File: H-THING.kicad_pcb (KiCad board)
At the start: 2 copper layers, 18 parts, among them J1 MOTOR_CON, J2 PWR_PASSTHRU, J3 MAIN_PWR, J4 SIG_CON, Q1 2N3904, Q2 IRF5305, Q3 HUF75321, Q4 IRF5305, Q5 HUF75321, Q6 2N3904

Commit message: Layed out PCB
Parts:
- removed R3: 0R00, Resistors_THT:R_Axial_DIN0207_L6.3mm_D2.5mm_P2.54mm_Vertical
- added R6: 0R20, Resistors_THT:R_Axial_DIN0207_L6.3mm_D2.5mm_P2.54mm_Vertical, F.Cu at (161.8, 112.0)
- added REF**: MountingHole_3.2mm_M3, Mounting_Holes:MountingHole_3.2mm_M3, F.Cu at (168.8, 113.5)
- added REF**: MountingHole_3.2mm_M3, Mounting_Holes:MountingHole_3.2mm_M3, F.Cu at (168.8, 91.4)
- added REF**: MountingHole_3.2mm_M3, Mounting_Holes:MountingHole_3.2mm_M3, F.Cu at (143.4, 113.4)
- added REF**: MountingHole_3.2mm_M3, Mounting_Holes:MountingHole_3.2mm_M3, F.Cu at (143.5, 91.4)
- C1, C3: footprint Capacitors_THT:C_Disc_D3.4mm_W2.1mm_P2.50mm -> Capacitors_THT:C_Disc_D5.0mm_W2.5mm_P5.00mm
- C2: footprint Capacitors_SMD:CP_Elec_8x10.5 -> Capacitors_THT:CP_Radial_D10.0mm_P5.00mm
- J1, J2, J3: footprint TerminalBlocks_Phoenix:TerminalBlock_Phoenix_MPT-2.54mm_2pol -> Connectors_Terminal_Blocks:TerminalBlock_bornier-2_P5.08mm
- J4: footprint Connectors_JST:JST_XH_B03B-XH-A_03x2.50mm_Straight -> Socket_Strips:Socket_Strip_Straight_1x03_Pitch2.54mm
- Q1, Q6: footprint TO_SOT_Packages_THT:TO-92_Molded_Narrow -> TO_SOT_Packages_THT:TO-92_Inline_Narrow_Oval
- Q2, Q3, Q4, Q5: footprint TO_SOT_Packages_THT:TO-220-3_Horizontal -> TO_SOT_Packages_THT:TO-220-3_Vertical
- R2, R4: value 3k30 -> 1k00
- moved Q1 33.1 mm to (157.1, 114.0), turned to 90 degrees
- moved C1 32.2 mm to (149.4, 100.5), turned to 270 degrees
- moved R1 31.4 mm to (151.4, 114.4), turned to 180 degrees
- moved J3 31.1 mm to (175.5, 113.5)
- moved J1 29.3 mm to (143.5, 100.3), turned to 270 degrees
- moved C2 29.1 mm to (175.6, 103.9)
- moved C3 28.7 mm to (175.6, 96.8)
- moved J2 27.2 mm to (180.6, 90.9), turned to 180 degrees
- moved Q3 26.2 mm to (169.7, 105.2), turned to 180 degrees
- moved R2 21.1 mm to (149.4, 111.0), turned to 0 degrees
- moved Q5 17.3 mm to (164.6, 100.6), turned to 0 degrees
- moved J4 14.5 mm to (162.8, 89.8)
- moved Q2 12.5 mm to (159.0, 105.2), turned to 180 degrees
- moved Q6 7.87 mm to (150.7, 90.9), turned to 270 degrees
- moved R5 7.10 mm to (157.9, 90.3), turned to 180 degrees
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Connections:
- J1 pad 1: Net-(C1-Pad2) -> Net-(C1-Pad1)
- J1 pad 2: Net-(C1-Pad1) -> Net-(C1-Pad2)
- J2 pad 1: VCC -> GND
- J2 pad 2: GND -> VCC
- J4 pad 2: GND -> /I_SENSE
- Q3 pad 3: GND -> /I_SENSE
- Q5 pad 3: GND -> /I_SENSE
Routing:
- net VCC: track 0.00 -> 63.3 mm
- net /HB1: track 0.00 -> 42.0 mm
- net Net-(C1-Pad1): track 0.00 -> 31.7 mm
- net Net-(C1-Pad2): track 0.00 -> 31.6 mm
- net /I_SENSE: track 0.00 -> 27.8 mm
- net Net-(Q1-Pad3): track 0.00 -> 25.8 mm
- net Net-(Q4-Pad1): track 0.00 -> 24.9 mm
- net /HB2: track 0.00 -> 6.85 mm
- net Net-(Q1-Pad2): track 0.00 -> 6.40 mm
- net Net-(Q6-Pad2): track 0.00 -> 5.36 mm
- added copper zone on B.Cu, net GND
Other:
- board outline added: 44.6 x 31 mm

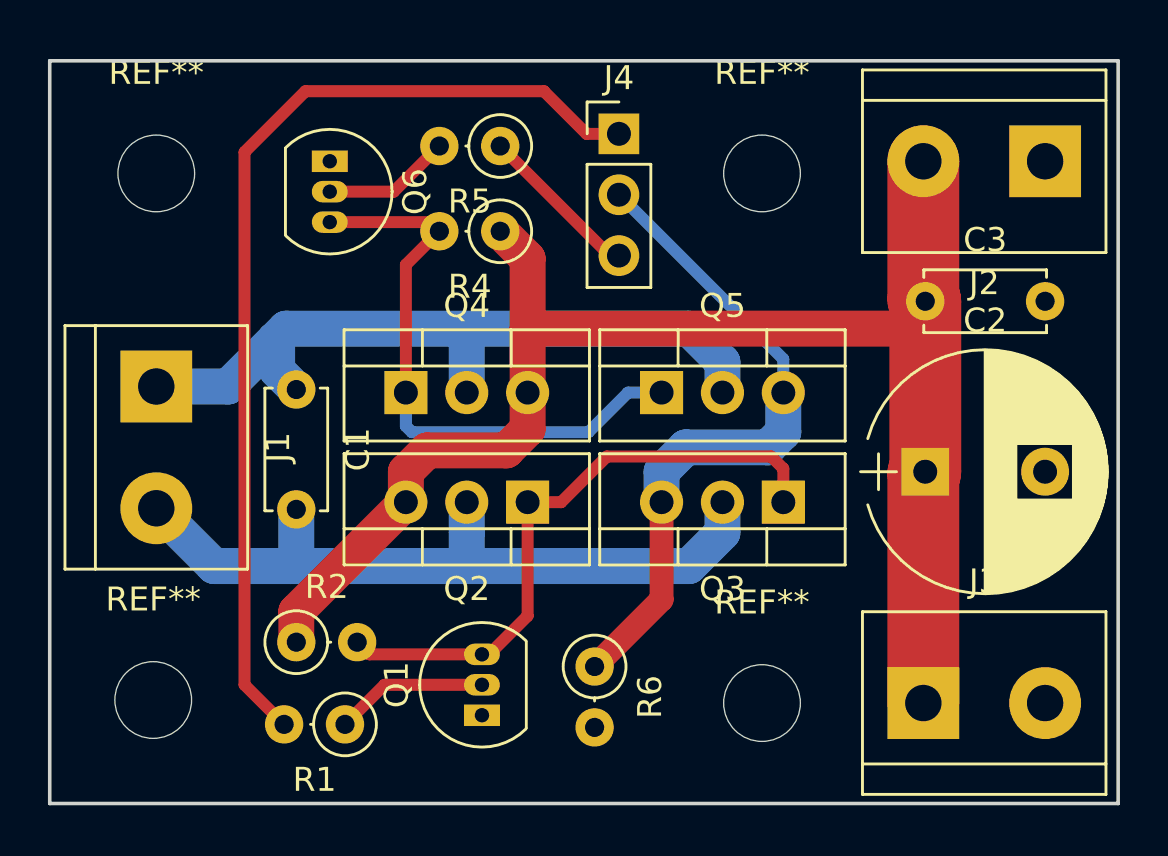
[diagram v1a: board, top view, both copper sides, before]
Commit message: Added images
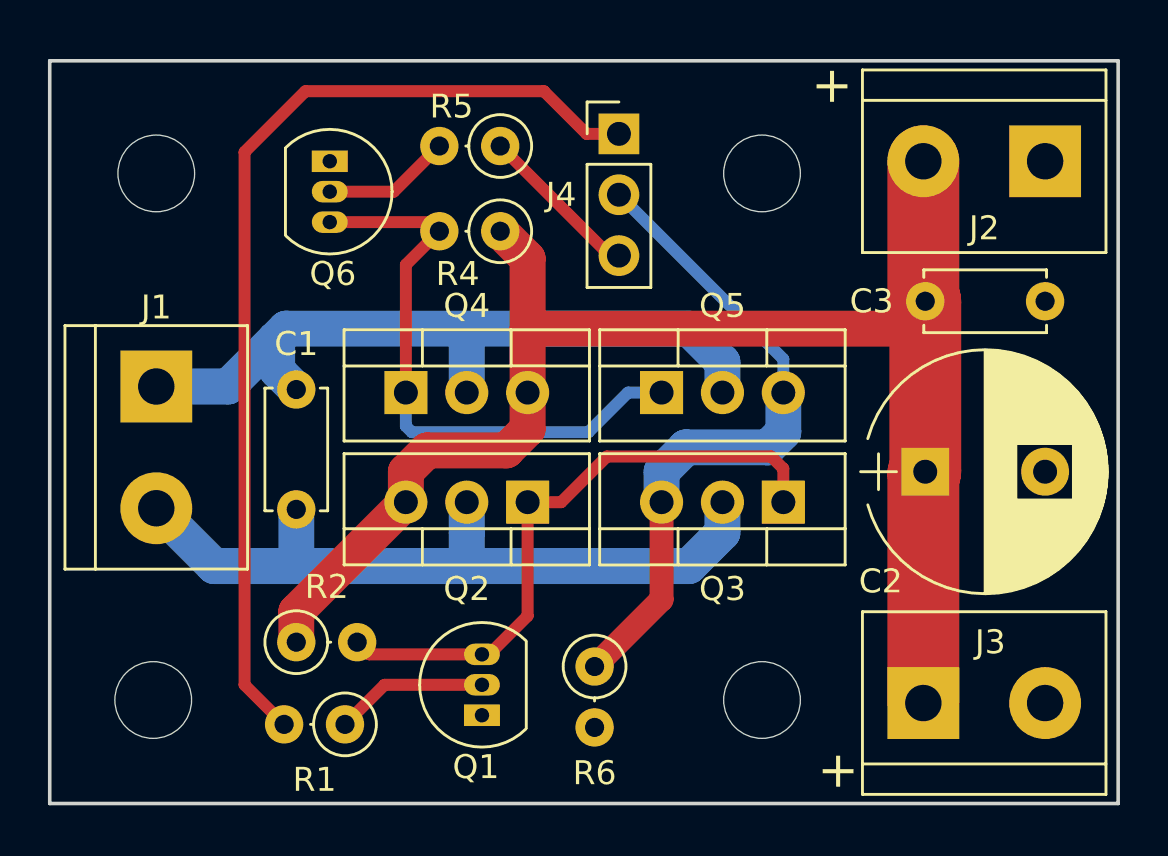
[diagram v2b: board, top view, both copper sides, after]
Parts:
- added G***: LOGO, footprints:rover, B.Cu at (161.9, 108.8)
- moved MH3 0.13 mm to (168.8, 113.4)
- turned MH1 to 180 degrees
- turned MH2 to 180 degrees
- renumbered REF** to MH1, REF** to MH2, REF** to MH3, REF** to MH4
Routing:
- added copper zone on F.Cu, net GND
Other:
- board text added: "+"
- board text added: "H-THING (H-Bridge) by Vlad Pomogaev"

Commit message: Added propper grbr outputs
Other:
- board text added: "MOTOR"
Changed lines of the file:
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@@
   (general
     (thickness 1.6)
-    (drawings 12)
+    (drawings 13)
     (tracks 79)
     (zones 0)
@@
   (page A4)
   (layers
-    (0 F.Cu signal)
-    (31 B.Cu signal)
+    (0 F.Cu signal hide)
+    (31 B.Cu signal hide)
     (32 B.Adhes user)
     (33 F.Adhes user)
@@
     (pad_to_mask_clearance 0.2)
     (aux_axis_origin 0 0)
-    (visible_elements 7FFEEFFF)
+    (visible_elements 7FFFEFFF)
     (pcbplotparams
-      (layerselection 0x00030_80000001)
+      (layerselection 0x010f0_ffffffff)
       (usegerberextensions false)
       (usegerberattributes false)
@@
       (outputformat 1)
       (mirror false)
-      (drillshape 1)
+      (drillshape 0)
       (scaleselection 1)
       (outputdirectory ""))
@@
       (xy -1.910234 -1.966072) (xy -1.841807 -1.920478) (xy -1.827096 -1.934329)) (layer B.SilkS) (width 0.01))
   )
+  (gr_text MOTOR (at 143.5354 109.1438) (layer F.SilkS)
+    (effects (font (size 1.5 1.5) (thickness 0.3)))
+  )
   (dimension 14.732 (width 0.3) (layer Dwgs.User)

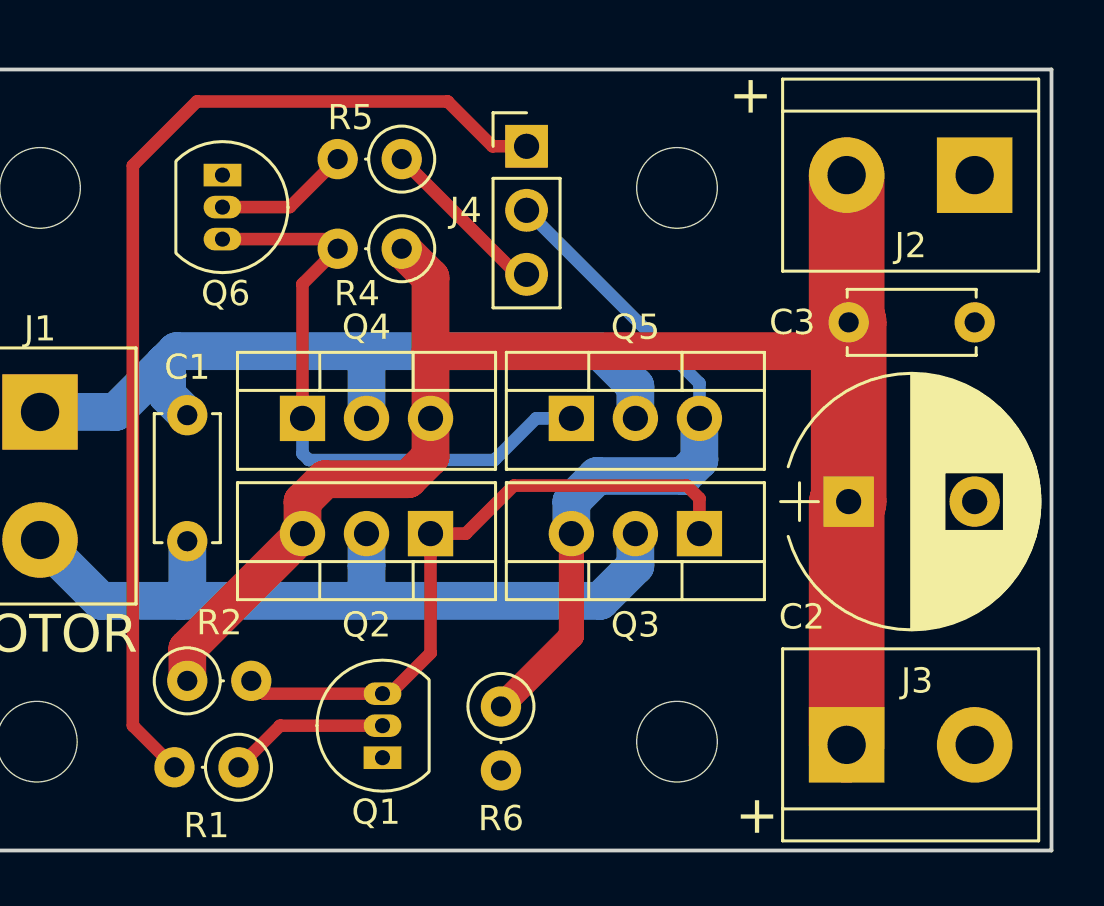
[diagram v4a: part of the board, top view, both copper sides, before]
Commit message: Updated 3d model with components
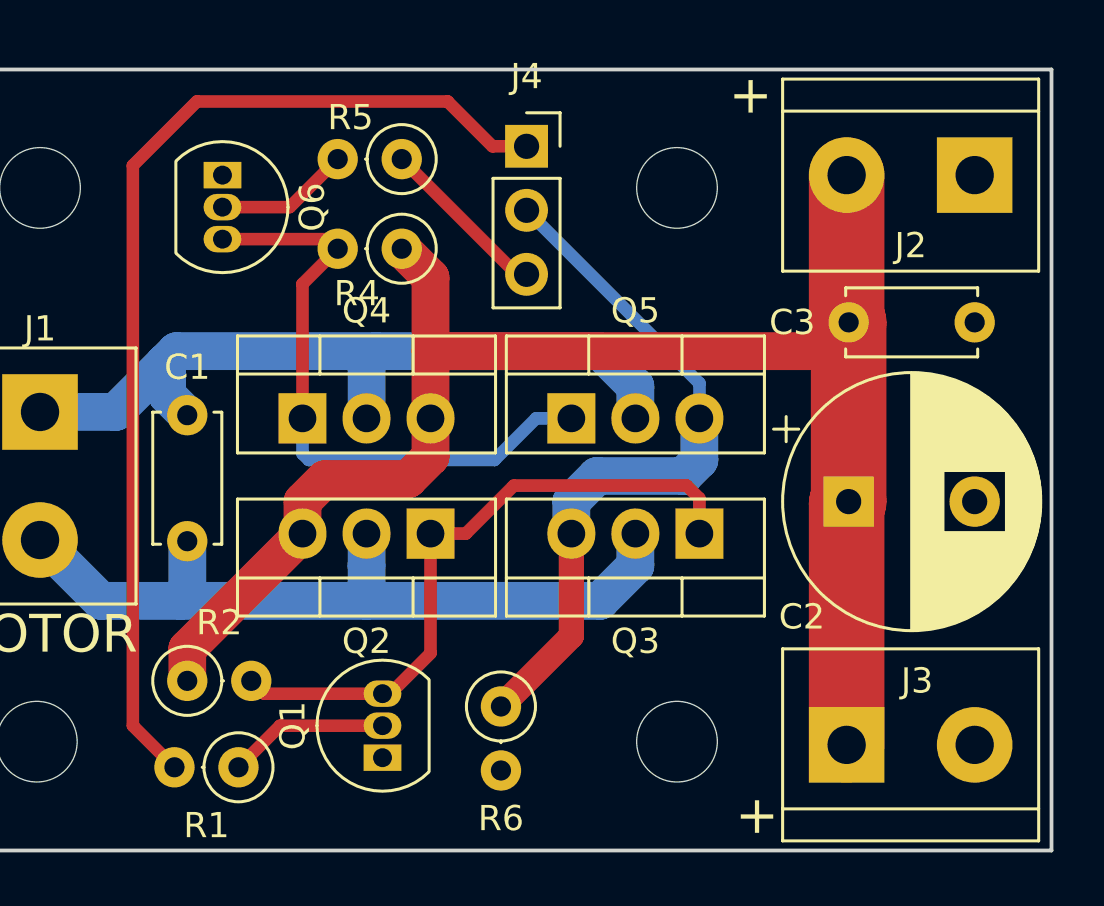
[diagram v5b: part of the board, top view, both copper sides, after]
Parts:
- C1, C3: footprint Capacitors_THT:C_Disc_D5.0mm_W2.5mm_P5.00mm -> Capacitor_THT:C_Disc_D5.0mm_W2.5mm_P5.00mm
- C2: footprint Capacitors_THT:CP_Radial_D10.0mm_P5.00mm -> Capacitor_THT:CP_Radial_D10.0mm_P5.00mm
- J1, J2, J3: footprint Connectors_Terminal_Blocks:TerminalBlock_bornier-2_P5.08mm -> TerminalBlock:TerminalBlock_bornier-2_P5.08mm
- J4: footprint Socket_Strips:Socket_Strip_Straight_1x03_Pitch2.54mm -> Connector_PinSocket_2.54mm:PinSocket_1x03_P2.54mm_Vertical
- Q1, Q6: footprint TO_SOT_Packages_THT:TO-92_Inline_Narrow_Oval -> Package_TO_SOT_THT:TO-92_Inline
- Q2, Q3, Q4, Q5: footprint TO_SOT_Packages_THT:TO-220-3_Vertical -> Package_TO_SOT_THT:TO-220-3_Vertical
- R1, R2, R4, R5, R6: footprint Resistors_THT:R_Axial_DIN0207_L6.3mm_D2.5mm_P2.54mm_Vertical -> Resistor_THT:R_Axial_DIN0207_L6.3mm_D2.5mm_P2.54mm_Vertical
